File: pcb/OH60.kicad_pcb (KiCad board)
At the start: 2 copper layers, 134 parts, among them SW1 SW_SPST, SW10 SW_SPST, SW11 SW_SPST, SW12 SW_SPST, SW13 SW_SPST, SW14 SW_SPST, SW15 SW_SPST, SW16 SW_SPST, SW17 SW_SPST, SW18 SW_SPST, SW19 SW_SPST, SW2 SW_SPST, SW20 SW_SPST, SW21 SW_SPST, SW22 SW_SPST, SW23 SW_SPST, SW24 SW_SPST, SW25 SW_SPST, SW26 SW_SPST, SW27 SW_SPST, SW28 SW_SPST, SW29 SW_SPST, SW3 SW_SPST, SW30 SW_SPST, SW31 SW_SPST, SW32 SW_SPST, SW33 SW_SPST, SW34 SW_SPST, SW35 SW_SPST, SW36 SW_SPST, SW37 SW_SPST, SW38 SW_SPST, SW39 SW_SPST, SW4 SW_SPST, SW40 SW_SPST, SW41 SW_SPST, SW42 SW_SPST, SW43 SW_SPST, SW44 SW_SPST, SW45 SW_SPST, SW46 SW_SPST, SW47 SW_SPST, SW48 SW_SPST, SW49 SW_SPST, SW5 SW_SPST, SW50 SW_SPST, SW51 SW_SPST, SW52 SW_SPST, SW53 SW_SPST, SW54 SW_SPST, SW55 SW_SPST, SW56 SW_SPST, SW57 SW_SPST, SW58 SW_SPST, SW59 SW_SPST, SW6 SW_SPST, SW60 SW_SPST, SW61 SW_SPST, SW62 SW_SPST, SW63 SW_SPST, SW64 SW_SPST, SW65 SW_SPST, SW66 SW_SPST, SW67 SW_SPST, SW7 SW_SPST, SW8 SW_SPST, SW9 SW_SPST

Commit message: Finished with initial layout of matrix
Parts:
- removed D62, D63, D64, D65, D66, D67: D_ALT, Diode_SMD:D_0805_2012Metric
- removed SW62, SW63, SW64, SW65, SW66, SW67: SW_SPST, Keyboard:CHERRY_PCB_100H
- D1, D10, D11, D12, D13, D14, D15, D16, D17, D18, D19, D2, D20, D21, D22, D23, D24, D25, D26, D27, D28, D29, D3, D30, D31, D32, D33, D34, D35, D36, D37, D38, D39, D4, D40, D41, D42, D43, D44, D45, D46, D47, D48, D49, D5, D50, D51, D52, D53, D54, D55, D56, D57, D58, D59, D6, D60, D61, D7, D8, D9: footprint Diode_SMD:D_0805_2012Metric -> Diode_SMD:D_SOD-123; moved to B.Cu
- SW29: footprint Keyboard:CHERRY_PCB_100H -> Keyboard:CHERRY_PCB_175H
- SW41: footprint Keyboard:CHERRY_PCB_100H -> Keyboard:CHERRY_PCB_225H
- SW42: footprint Keyboard:CHERRY_PCB_150H -> Keyboard:CHERRY_PCB_225H
- SW54, SW55, SW56, SW58, SW59, SW60, SW61: footprint Keyboard:CHERRY_PCB_100H -> Keyboard:CHERRY_PCB_125H
- SW57: footprint Keyboard:CHERRY_PCB_100H -> Keyboard:CHERRY_PCB_625H
- moved D28 376.8 mm to (301.9, 50.0)
- moved D14 375.6 mm to (297.2, 31.0)
- moved D13 370.6 mm to (268.6, 31.0)
- moved D41 367.3 mm to (294.8, 69.1)
- moved D27 360.3 mm to (278.1, 50.0)
- moved D12 355.8 mm to (249.6, 31.0)
- moved D61 354.6 mm to (309.3, 107.2)
- moved D53 350.1 mm to (290.0, 88.2)
- moved D26 347.8 mm to (259.1, 50.0)
- moved D11 343.8 mm to (230.5, 31.0)
- moved D25 336.2 mm to (240.0, 50.0)
- moved D24 335.5 mm to (221.0, 50.0)
- moved D40 335.2 mm to (263.8, 69.1)
- moved D39 333.2 mm to (244.8, 69.1)
- moved D10 332.9 mm to (211.4, 31.0)
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
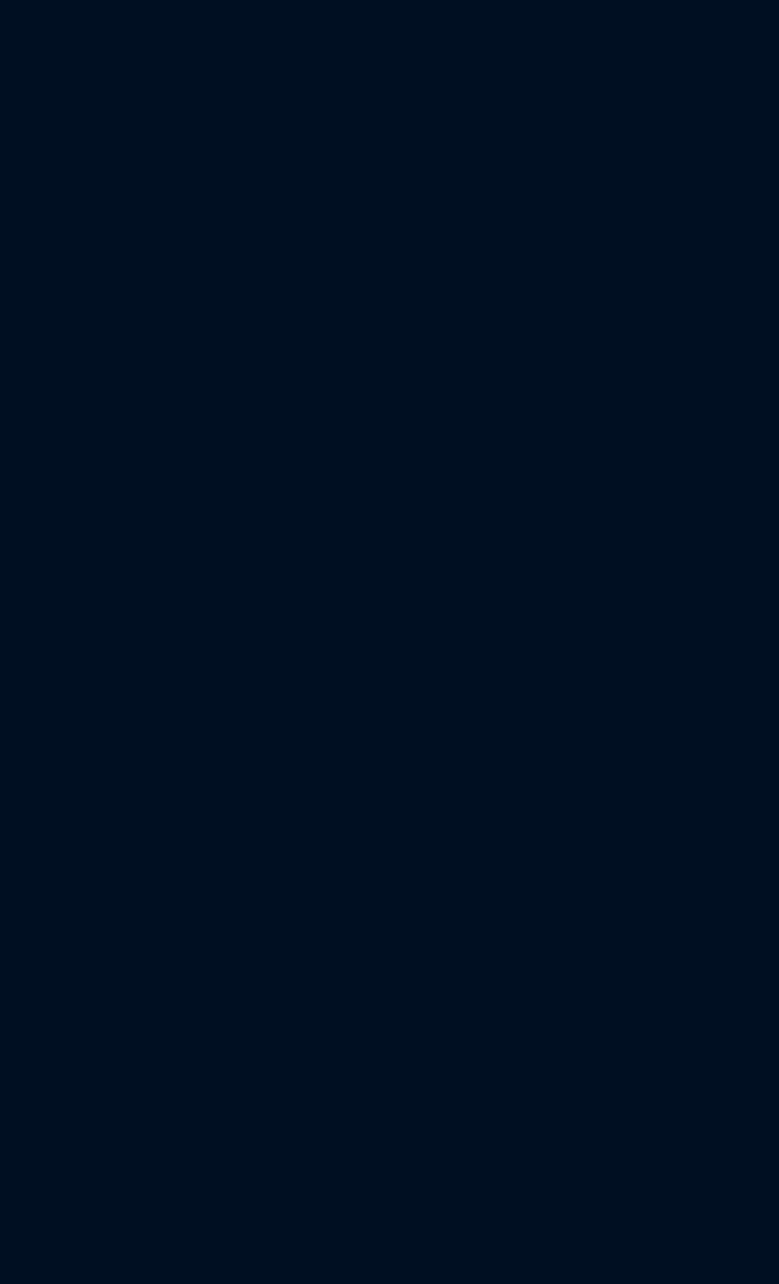
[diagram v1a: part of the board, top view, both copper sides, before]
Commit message: Started adding MCU
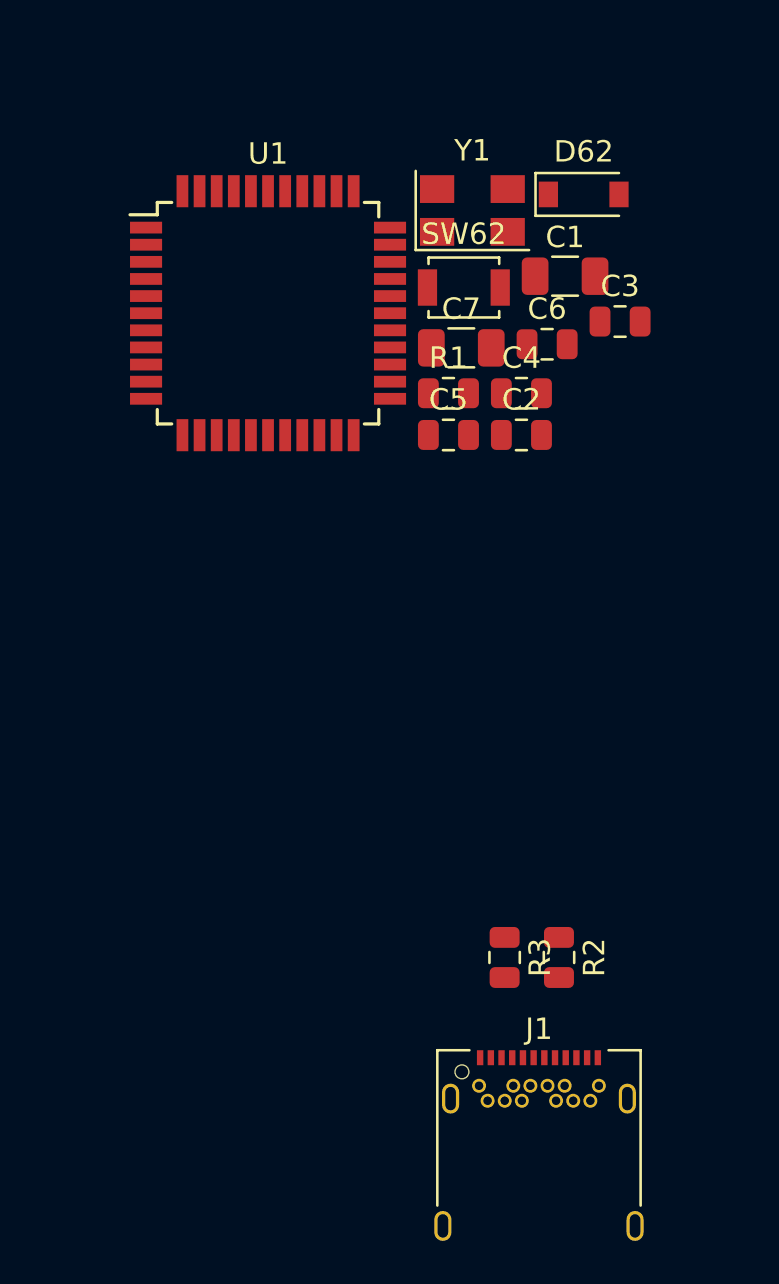
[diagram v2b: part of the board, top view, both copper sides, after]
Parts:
- added C1: 1uF, Capacitor_SMD:C_1206_3216Metric, F.Cu at (202.2, 146.0)
- added C2: 100n, Capacitor_SMD:C_0805_2012Metric, F.Cu at (200.2, 153.4)
- added C3: 100n, Capacitor_SMD:C_0805_2012Metric, F.Cu at (204.8, 148.1)
- added C4: 22pF, Capacitor_SMD:C_0805_2012Metric, F.Cu at (200.2, 151.4)
- added C5: 22pF, Capacitor_SMD:C_0805_2012Metric, F.Cu at (196.8, 153.4)
- added C6: 100n, Capacitor_SMD:C_0805_2012Metric, F.Cu at (201.4, 149.1)
- added C7: 1uF, Capacitor_SMD:C_1206_3216Metric, F.Cu at (197.4, 149.3)
- added D62: 1n4148, Diode_SMD:D_SOD-123, F.Cu at (203.1, 142.1)
- added J1: USB_C_Receptacle_USB2.0, Connector_USB:USB_C_Receptacle_Amphenol_12401548E4-2A, F.Cu at (201.0, 187.5)
- added R1: 10k, Resistor_SMD:R_0805_2012Metric, F.Cu at (196.8, 151.4)
- added R2: 22R, Resistor_SMD:R_0805_2012Metric, F.Cu at (201.9, 177.8)
- added R3: 22R, Resistor_SMD:R_0805_2012Metric, F.Cu at (199.4, 177.8)
- added SW62: SW_Push, Button_Switch_SMD:SW_SPST_B3U-1000P, F.Cu at (197.5, 146.5)
- added U1: ATmega32U4-AU, Package_QFP:TQFP-44_10x10mm_P0.8mm, F.Cu at (188.3, 147.7)
- added Y1: 16MHz, Crystal:Crystal_SMD_5032-4Pin_5.0x3.2mm, F.Cu at (197.9, 142.9)

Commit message: Started routing a few tracks and minor matrix adjustments
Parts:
- removed SW62: SW_Push, Button_Switch_SMD:SW_SPST_B3U-1000P
- added C10: 22uF, Capacitor_SMD:C_0805_2012Metric, B.Cu at (217.2, 4.45)
- added C8: 1uF, Capacitor_SMD:C_1206_3216Metric, F.Cu at (203.4, 8.39)
- added C9: 100n, Capacitor_SMD:C_0805_2012Metric, F.Cu at (200.8, 10.4)
- added F1: MF-MSMF050-2, Fuse:Fuse_1812_4532Metric, F.Cu at (198.7, 7.44)
- added FB1: Ferrite_Bead, Resistor_SMD:R_0805_2012Metric, F.Cu at (203.4, 6.44)
- added J2: USB_B_Micro, Connector_USB:USB_Micro-B_Molex-105017-0001, F.Cu at (183.0, 30.2)
- added R4: 22R, Resistor_SMD:R_0805_2012Metric, F.Cu at (184.3, 34.9)
- added RESET_SW1: SW_Push, Button_Switch_SMD:SW_SPST_B3U-1000P, B.Cu at (172.8, 102.0)
- C1, C2, C3, C5, D62, R1, U1, Y1: moved to B.Cu
- C4: value 22pF -> 100n; moved to B.Cu
- C6: value 100n -> 22pF; moved to B.Cu
- C7: value 1uF -> 100n; footprint Capacitor_SMD:C_1206_3216Metric -> Capacitor_SMD:C_0805_2012Metric; moved to B.Cu
- J1: value USB_C_Receptacle_USB2.0 -> Conn_02x03_Odd_Even; footprint Connector_USB:USB_C_Receptacle_Amphenol_12401548E4-2A -> Connector_PinHeader_2.54mm:PinHeader_2x03_P2.54mm_Vertical
- R2: value 22R -> 10k; moved to B.Cu
- moved R2 144.3 mm to (179.4, 35.3), turned to 180 degrees
- moved R3 144.0 mm to (182.1, 34.9), turned to 90 degrees
- moved J1 76.3 mm to (170.7, 117.5)
- moved R1 53.0 mm to (180.7, 101.0)
- moved C5 51.6 mm to (185.5, 103.0), turned to 180 degrees
- moved C4 49.6 mm to (189.5, 103.0)
- moved D62 44.9 mm to (180.6, 103.3)
- moved Y1 44.2 mm to (187.5, 99.9), turned to 180 degrees
- moved C2 42.6 mm to (197.4, 110.9)
- moved C7 41.9 mm to (178.9, 111.6), turned to 270 degrees
- moved C1 37.6 mm to (197.9, 108.6)
- moved U1 35.9 mm to (188.0, 111.8)
- moved C6 33.3 mm to (184.6, 120.4), turned to 180 degrees
- moved C3 30.3 mm to (192.4, 120.4), turned to 180 degrees
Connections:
- C4 pad 1: Net-(C4-Pad1) -> +5V
- D62 pad 2: Net-(D62-Pad2) -> /mcu/RESET
- R1 pad 2: Net-(D62-Pad2) -> /mcu/RESET
- R2 pad 1: /mcu/D- -> GND
- R2 pad 2: Net-(J1-PadA7) -> +5V
- R3 pad 2: Net-(J1-PadA6) -> Net-(J2-Pad3)
- SW57 pad 2: /matrix/COL_3 -> /matrix/COL_5
- SW58 pad 2: /matrix/COL_4 -> /matrix/COL_9
- SW59 pad 2: /matrix/COL_5 -> /matrix/COL_10
- SW60 pad 2: /matrix/COL_6 -> /matrix/COL_11
- SW61 pad 2: /matrix/COL_7 -> /matrix/COL_12
- U1 pad 10: Net-(U1-Pad10) -> /mcu/MOSI
- U1 pad 11: Net-(U1-Pad11) -> /mcu/MISO
- U1 pad 12: Net-(U1-Pad12) -> /matrix/COL_4
- U1 pad 13: Net-(D62-Pad2) -> /mcu/RESET
- U1 pad 16: Net-(C5-Pad1) -> Net-(C6-Pad1)
- U1 pad 17: Net-(C4-Pad1) -> Net-(C5-Pad1)
- U1 pad 18: Net-(U1-Pad18) -> /matrix/COL_7
- U1 pad 19: Net-(U1-Pad19) -> /matrix/COL_8
- U1 pad 20: Net-(U1-Pad20) -> /matrix/COL_9
- U1 pad 21: Net-(U1-Pad21) -> /matrix/COL_10
- U1 pad 22: Net-(U1-Pad22) -> /matrix/COL_12
- U1 pad 25: Net-(U1-Pad25) -> /matrix/COL_11
- U1 pad 26: Net-(U1-Pad26) -> /matrix/COL_13
- U1 pad 28: Net-(U1-Pad28) -> /matrix/COL_1
- U1 pad 29: Net-(U1-Pad29) -> /matrix/COL_2
- U1 pad 30: Net-(U1-Pad30) -> /matrix/COL_3
- U1 pad 31: Net-(U1-Pad31) -> /matrix/COL_5
- U1 pad 32: Net-(U1-Pad32) -> /matrix/COL_6
- U1 pad 37: Net-(U1-Pad37) -> /matrix/ROW_4
- U1 pad 38: Net-(U1-Pad38) -> /matrix/ROW_3
- U1 pad 39: Net-(U1-Pad39) -> /matrix/ROW_2
- U1 pad 40: Net-(U1-Pad40) -> /matrix/ROW_1
- U1 pad 41: Net-(U1-Pad41) -> /matrix/ROW_0
- U1 pad 42: Net-(C6-Pad1) -> Net-(C7-Pad1)
- U1 pad 6: Net-(C7-Pad1) -> Net-(C8-Pad1)
- U1 pad 8: Net-(U1-Pad8) -> /matrix/COL_0
- U1 pad 9: Net-(U1-Pad9) -> /mcu/SCK
- Y1 pad 1: Net-(C4-Pad1) -> Net-(C5-Pad1)
- Y1 pad 3: Net-(C5-Pad1) -> Net-(C6-Pad1)
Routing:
- net /matrix/ROW_0: track 0.00 -> 284.5 mm
- net /matrix/ROW_2: track 0.00 -> 272.7 mm
- net /matrix/ROW_3: track 0.00 -> 262.5 mm
- net /matrix/ROW_1: track 0.00 -> 237.4 mm
- net /matrix/ROW_4: track 0.00 -> 116.2 mm
- net /matrix/COL_11: track 0.00 -> 107.5 mm, vias 0 -> 1
- net /matrix/COL_1: track 0.00 -> 104.1 mm, vias 0 -> 1
- net /matrix/COL_12: track 0.00 -> 102.7 mm, vias 0 -> 3
- net /matrix/COL_2: track 0.00 -> 95.6 mm, vias 0 -> 1
- net /matrix/COL_0: track 0.00 -> 87.7 mm
- net /matrix/COL_5: track 0.00 -> 87.2 mm
- net /matrix/COL_10: track 0.00 -> 87.0 mm
- net /matrix/COL_3: track 0.00 -> 67.6 mm
- net /matrix/COL_8: track 0.00 -> 67.0 mm
- net /matrix/COL_7: track 0.00 -> 67.0 mm
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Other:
- board outline added: 285.8 x 100.7 mm
- net class Default: clearance 0.2 -> 0.1524; trace_width 0.25 -> 0.1524; via_dia 0.8 -> 0.6858; via_drill 0.4 -> 0.3302
- rule pad_to_mask_clearance: 0.051 -> 0.0508
- rule trace_clearance: 0.2 -> 0.1524
- rule trace_min: 0.2 -> 0.1524
- rule via_min_drill: 0.3 -> 0.254
- rule via_min_size: 0.4 -> 0.508

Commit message: Continued adding a few tracks for the matrix
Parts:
- added C11: 100n, Capacitor_SMD:C_0805_2012Metric, B.Cu at (177.7, 109.5)
- added C12: 22uF, Capacitor_SMD:C_0805_2012Metric, B.Cu at (191.7, 34.5)
- C10: value 22uF -> 1uF; footprint Capacitor_SMD:C_0805_2012Metric -> Capacitor_SMD:C_1206_3216Metric
- C5, C6: value 22pF -> 100n
- C7: value 100n -> 22pF
- C8: value 1uF -> 22pF; footprint Capacitor_SMD:C_1206_3216Metric -> Capacitor_SMD:C_0805_2012Metric; moved to B.Cu
- C9: moved to B.Cu
- moved C10 114.8 mm to (177.2, 112.0), turned to 180 degrees
- moved C9 112.2 mm to (183.9, 121.3), turned to 180 degrees
- moved C8 96.8 mm to (185.3, 103.5), turned to 180 degrees
- moved C5 68.4 mm to (188.2, 34.7)
- moved FB1 35.8 mm to (177.0, 30.7), turned to 270 degrees
- moved J1 34.7 mm to (205.0, 122.8), turned to 270 degrees
- moved F1 24.7 mm to (190.8, 30.9), turned to 180 degrees
- moved C4 16.9 mm to (177.8, 115.2), turned to 180 degrees
- moved C6 16.8 mm to (180.4, 104.1)
- moved C7 13.5 mm to (189.7, 103.5), turned to 0 degrees
- moved R1 9.73 mm to (173.4, 107.3), turned to 180 degrees
- moved D62 7.58 mm to (173.2, 105.0), turned to 180 degrees
- moved C2 4.58 mm to (198.5, 106.4)
- moved R4 1.85 mm to (184.8, 36.7)
- moved R3 1.78 mm to (182.0, 36.7)
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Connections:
- net Net-(J2-Pad2) renamed /mcu/PRE_D-
- net Net-(J2-Pad3) renamed /mcu/PRE_D+
- C5 pad 1: Net-(C5-Pad1) -> +5V
- C6 pad 1: Net-(C6-Pad1) -> +5V
- C9 pad 1: +5V -> Net-(C9-Pad1)
- F1 pad 2: Net-(C10-Pad1) -> Net-(C12-Pad1)
- J2 pad 1: Net-(C10-Pad1) -> Net-(C12-Pad1)
- U1 pad 1: Net-(U1-Pad1) -> /matrix/COL_5
- U1 pad 12: /matrix/COL_4 -> /matrix/ROW_4
- U1 pad 16: Net-(C6-Pad1) -> Net-(C8-Pad1)
- U1 pad 17: Net-(C5-Pad1) -> Net-(C7-Pad1)
- U1 pad 26: /matrix/COL_13 -> /matrix/ROW_0
- U1 pad 28: /matrix/COL_1 -> /matrix/ROW_1
- U1 pad 29: /matrix/COL_2 -> /matrix/ROW_2
- U1 pad 30: /matrix/COL_3 -> /matrix/ROW_3
- U1 pad 31: /matrix/COL_5 -> Net-(U1-Pad31)
- U1 pad 32: /matrix/COL_6 -> /matrix/COL_13
- U1 pad 37: /matrix/ROW_4 -> /matrix/COL_0
- U1 pad 38: /matrix/ROW_3 -> /matrix/COL_1
- U1 pad 39: /matrix/ROW_2 -> /matrix/COL_2
- U1 pad 40: /matrix/ROW_1 -> /matrix/COL_3
- U1 pad 41: /matrix/ROW_0 -> /matrix/COL_4
- U1 pad 42: Net-(C7-Pad1) -> Net-(C9-Pad1)
- U1 pad 6: Net-(C8-Pad1) -> Net-(C10-Pad1)
- U1 pad 8: /matrix/COL_0 -> /matrix/COL_6
- Y1 pad 1: Net-(C5-Pad1) -> Net-(C7-Pad1)
- Y1 pad 3: Net-(C6-Pad1) -> Net-(C8-Pad1)
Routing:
- net /matrix/COL_13: track 21.0 -> 198.6 mm, vias 0 -> 3
- net /matrix/COL_0: track 87.7 -> 259.0 mm, vias 0 -> 2
- net /matrix/COL_1: track 104.1 -> 241.7 mm
- net /matrix/COL_2: track 95.6 -> 207.8 mm
- net /matrix/COL_3: track 67.6 -> 166.9 mm, vias 0 -> 1
- net GND: track 0.00 -> 86.1 mm, vias 0 -> 3
- net /matrix/COL_4: track 67.0 -> 146.8 mm, vias 0 -> 1
- net +5V: track 0.00 -> 56.7 mm, vias 0 -> 5
- net /matrix/ROW_4: track 116.2 -> 151.9 mm, vias 0 -> 4
- net /matrix/COL_5: track 87.2 -> 113.8 mm
- net /matrix/COL_6: track 67.0 -> 87.1 mm, vias 0 -> 1
- net Net-(C12-Pad1): track 0.00 -> 11.3 mm, vias 0 -> 1
- net /mcu/RESET: track 0.00 -> 10.6 mm, vias 0 -> 3
- net Net-(C8-Pad1): track 0.00 -> 8.99 mm
- net Net-(C7-Pad1): track 0.00 -> 5.39 mm
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
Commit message: Continued adding some tracks around the MCU
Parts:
- moved J1 1.81 mm to (203.6, 121.7)
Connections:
- U1 pad 12: /matrix/ROW_4 -> Net-(U1-Pad12)
- U1 pad 18: /matrix/COL_7 -> Net-(U1-Pad18)
- U1 pad 19: /matrix/COL_8 -> /matrix/COL_7
- U1 pad 20: /matrix/COL_9 -> /matrix/COL_8
- U1 pad 21: /matrix/COL_10 -> /matrix/ROW_0
- U1 pad 22: /matrix/COL_12 -> /matrix/ROW_1
- U1 pad 25: /matrix/COL_11 -> /matrix/ROW_2
- U1 pad 26: /matrix/ROW_0 -> /matrix/ROW_3
- U1 pad 27: Net-(U1-Pad27) -> /matrix/ROW_4
- U1 pad 28: /matrix/ROW_1 -> /matrix/COL_9
- U1 pad 29: /matrix/ROW_2 -> /matrix/COL_10
- U1 pad 30: /matrix/ROW_3 -> /matrix/COL_11
- U1 pad 31: Net-(U1-Pad31) -> /matrix/COL_12
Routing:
- net /matrix/ROW_4: track 151.9 -> 269.2 mm, vias 4 -> 3
- net /matrix/COL_12: track 102.7 -> 215.7 mm
- net /matrix/ROW_0: track 284.5 -> 375.5 mm, vias 0 -> 4
- net /matrix/COL_11: track 107.5 -> 196.5 mm
- net /matrix/ROW_1: track 237.4 -> 314.7 mm, vias 0 -> 4
- net /matrix/COL_10: track 87.0 -> 151.9 mm
- net /matrix/ROW_2: track 272.7 -> 333.8 mm, vias 0 -> 4
- net /matrix/COL_9: track 67.0 -> 123.6 mm
- net /matrix/ROW_3: track 262.5 -> 313.4 mm, vias 0 -> 2
- net GND: track 86.1 -> 135.8 mm, vias 3 -> 7
- net /matrix/COL_8: track 67.0 -> 99.4 mm, vias 0 -> 2
- net /matrix/COL_7: track 67.0 -> 89.3 mm, vias 0 -> 2
- net +5V: track 56.7 -> 78.9 mm, vias 5 -> 7
- net /mcu/RESET: track 10.6 -> 24.5 mm
- net Net-(U1-Pad12): track 0.00 -> 0.59 mm

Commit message: Mostly finished laying out the basic tracks
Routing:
- net GND: track 135.8 -> 306.8 mm, vias 7 -> 12
- net +5V: track 78.9 -> 213.5 mm, vias 7 -> 14
- net /mcu/D-: track 0.00 -> 90.7 mm, vias 0 -> 1
- net /mcu/D+: track 0.00 -> 90.2 mm, vias 0 -> 1
- net /matrix/ROW_1: track 314.7 -> 364.4 mm
- net /mcu/SCK: track 0.00 -> 34.0 mm, vias 0 -> 1
- net /mcu/MISO: track 0.00 -> 28.5 mm, vias 0 -> 1
- net /mcu/MOSI: track 0.00 -> 26.7 mm, vias 0 -> 1
- net /mcu/RESET: track 24.5 -> 46.9 mm, vias 3 -> 4
- net /matrix/ROW_4: track 269.2 -> 284.7 mm, vias 3 -> 6
- net /mcu/PRE_D-: track 0.02 -> 4.52 mm
- net /mcu/PRE_D+: track 0.00 -> 4.45 mm
- net /matrix/COL_7: track 89.3 -> 85.9 mm
- net /matrix/ROW_0: track 375.5 -> 374.6 mm

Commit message: Added mounting holes to the PCB
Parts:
- added MH1: MountingHole, MountingHole:MountingHole_2.2mm_M2, F.Cu at (55.9, 55.5)
- added MH2: MountingHole, MountingHole:MountingHole_2.2mm_M2, F.Cu at (32.9, 84.1)
- added MH3: MountingHole, MountingHole:MountingHole_2.2mm_M2, F.Cu at (159.1, 74.6)
- added MH4: MountingHole, MountingHole:MountingHole_2.2mm_M2, F.Cu at (221.4, 112.8)
- added MH5: MountingHole, MountingHole:MountingHole_2.2mm_M2, F.Cu at (290.9, 55.5)
- added MH6: MountingHole, MountingHole:MountingHole_2.2mm_M2, F.Cu at (313.9, 84.1)
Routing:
- net /matrix/COL_9: track 123.6 -> 125.4 mm
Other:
- board size 285.8 x 100.7 mm -> 285 x 99.3 mm

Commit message: Finished fixing silk-screen and zone-fills
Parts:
- added REF**: OSHW-Logo2_14.6x12mm_SilkScreen, Symbol:OSHW-Logo2_14.6x12mm_SilkScreen, B.Cu at (147.6, 111.9)
- C1, C10: value 1uF -> 1u
- moved C5 0.14 mm to (188.2, 34.5)
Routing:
- added copper zone on F.Cu, net +5V
- added copper zone on B.Cu, net GND
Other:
- board text added: "1"
- board text added: "E. Snyman"
- board text added: "ICSP"
- board text added: "OH60"
